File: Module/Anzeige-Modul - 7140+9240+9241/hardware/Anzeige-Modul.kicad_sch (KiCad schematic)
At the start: 53 parts, among them J1 Conn_01x09_Male, J3 Conn_02x03_Counter_Clockwise, J5 Conn_01x13_Male, J6 Conn_01x16_Male, Q11 BC847, Q21 BC847, Q31 BC847, Q41 BC847, Q51 BC847, Q61 BC847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

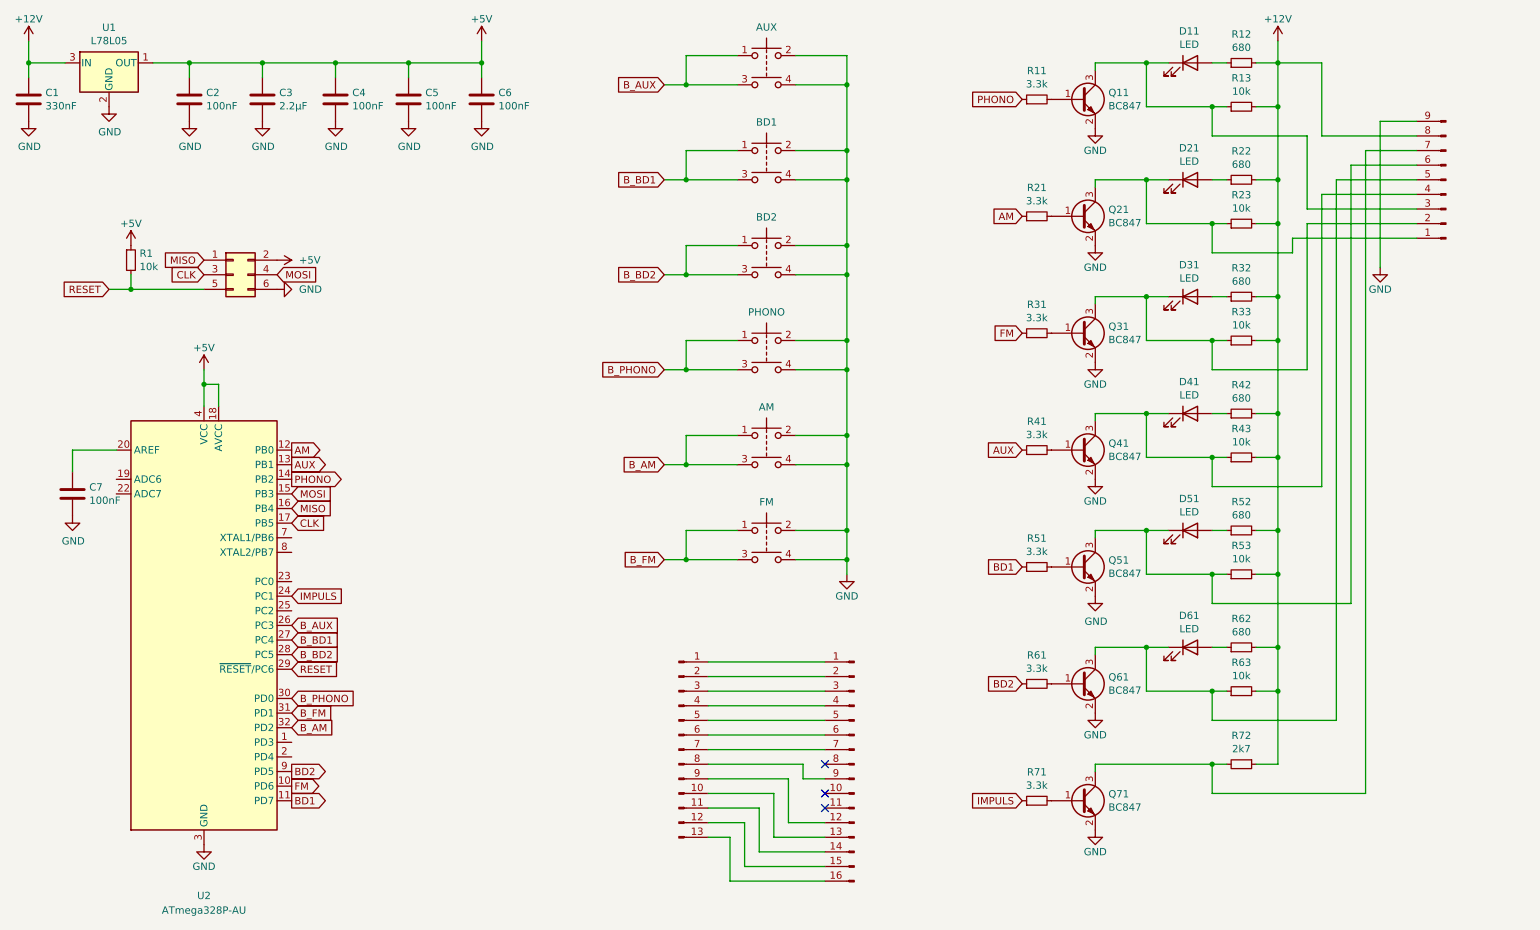
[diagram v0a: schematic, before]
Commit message: AZ553: LEDS added to BOM / Anzeige-Modul: Added additional Monting-Holes / Tipp-Tasten-Modul: Modified Push-Button Footprint
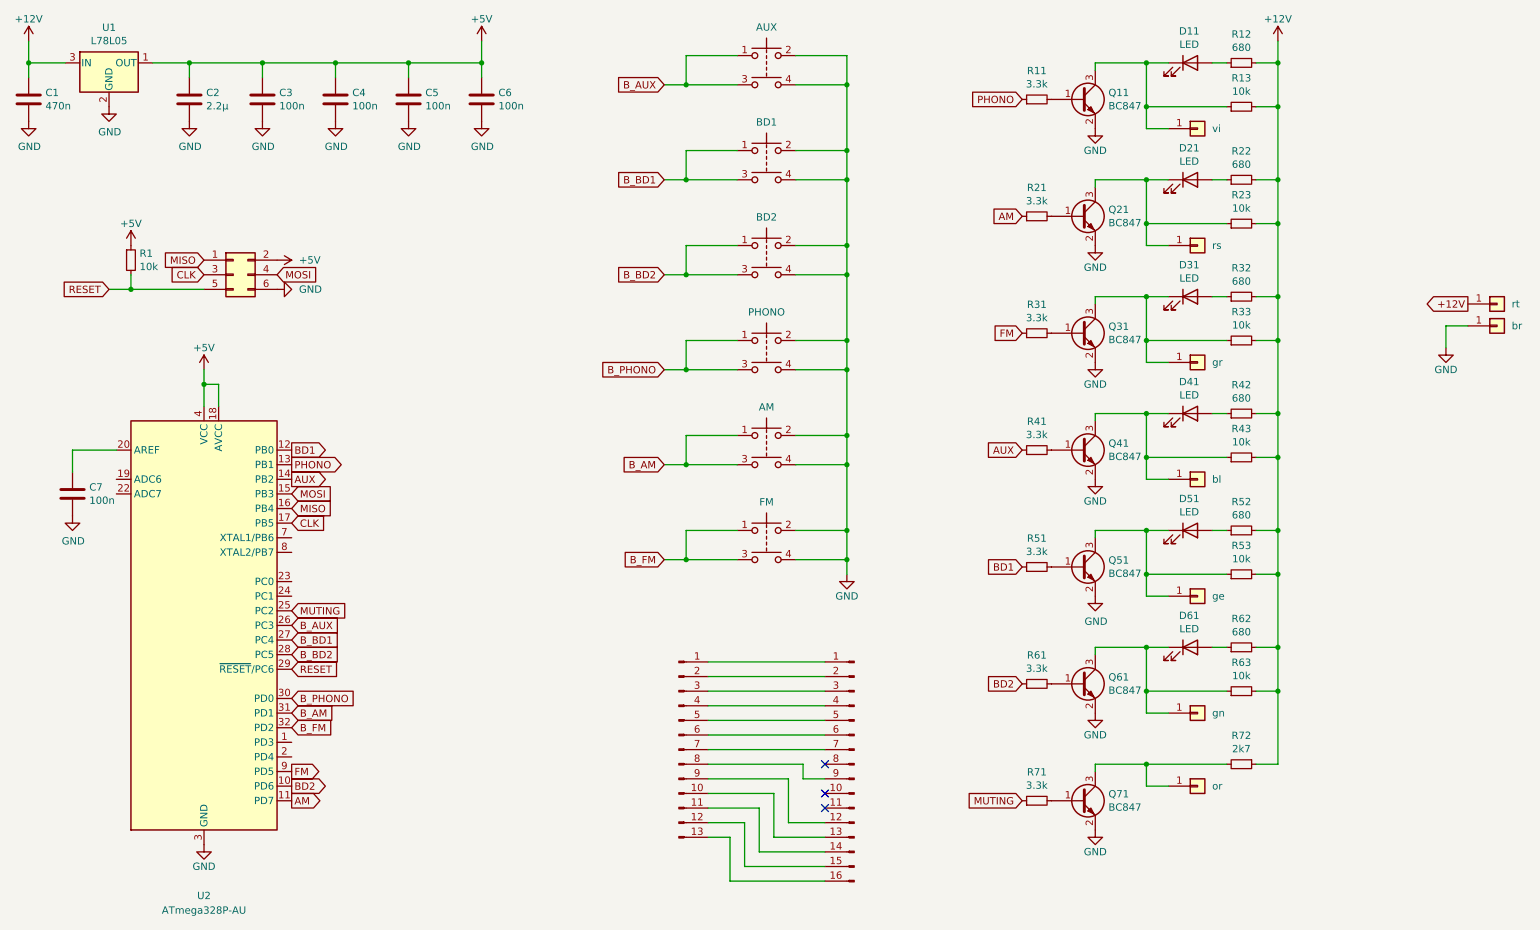
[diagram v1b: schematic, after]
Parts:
- removed J1: Conn_01x09_Male, Anzeige-Modul:PadArray_3.81mm_01x09, symbol Connector:Conn_01x09_Male
- added J10: gn, Anzeige-Modul:Conn_01x01, symbol Connector_Generic:Conn_01x01
- added J11: or, Anzeige-Modul:Conn_01x01, symbol Connector_Generic:Conn_01x01
- added J12: rt, Anzeige-Modul:Conn_01x01, symbol Connector_Generic:Conn_01x01
- added J13: br, Anzeige-Modul:Conn_01x01, symbol Connector_Generic:Conn_01x01
- added J2: vi, Anzeige-Modul:Conn_01x01, symbol Connector_Generic:Conn_01x01
- added J4: rs, Anzeige-Modul:Conn_01x01, symbol Connector_Generic:Conn_01x01
- added J7: gr, Anzeige-Modul:Conn_01x01, symbol Connector_Generic:Conn_01x01
- added J8: bl, Anzeige-Modul:Conn_01x01, symbol Connector_Generic:Conn_01x01
- added J9: ge, Anzeige-Modul:Conn_01x01, symbol Connector_Generic:Conn_01x01
- C1: value 330nF -> 470n; LCSC C1740 -> C13967
- C2: renamed from C3; value 2.2µF -> 2.2µ; LCSC C49217 -> C377773
- C3: renamed from C2; value 100nF -> 100n
- C4, C5, C6, C7: value 100nF -> 100n
- D11, D21, D31, D41, D51, D61: footprint LEDs:LED_Rectangular_W5.0mm_H2.0mm -> LED_THT:LED_Rectangular_W5.0mm_H2.0mm
- R62: footprint Resistors_SMD:R_0805 -> Resistor_SMD:R_0805_2012Metric
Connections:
- net +12V: now also J12.1 (Pin_1)
- net AM: now also U2.11 (PD7); no longer U2.12 (PB0)
- net AUX: now also U2.14 (PB2); no longer U2.13 (PB1)
- net BD1: now also U2.12 (PB0); no longer U2.11 (PD7)
- net BD2: now also U2.10 (PD6); no longer U2.9 (PD5)
- net B_AM: now also U2.31 (PD1); no longer U2.32 (PD2)
- net B_FM: now also U2.32 (PD2); no longer U2.31 (PD1)
- net FM: now also U2.9 (PD5); no longer U2.10 (PD6)
- net GND: now also J13.1 (Pin_1)
- net PHONO: now also U2.13 (PB1); no longer U2.14 (PB2)
- net at D11.1 (K), Q11.3 (C), R13.1: now also J2.1 (Pin_1)
- net at D21.1 (K), Q21.3 (C), R23.1: now also J4.1 (Pin_1)
- net at D31.1 (K), Q31.3 (C), R33.1: now also J7.1 (Pin_1)
- net at D41.1 (K), Q41.3 (C), R43.1: now also J8.1 (Pin_1)
- net at D51.1 (K), Q51.3 (C), R53.1: now also J9.1 (Pin_1)
- net at D61.1 (K), Q61.3 (C), R63.1: now also J10.1 (Pin_1)
- net at Q71.3 (C), R72.2: now also J11.1 (Pin_1)
- net MUTING: now reaches U2.25 (PC2)
- net MUTING: now also R71.1
- net IMPULS: no longer names the net of U2.24 (PC1)
- net IMPULS: no longer R71.1
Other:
- moved on the sheet: C2, C3
